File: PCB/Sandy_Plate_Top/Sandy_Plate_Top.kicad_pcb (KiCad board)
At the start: 2 copper layers, 285 x 37.6 mm, 21 parts

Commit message: Top用プレート作成（穴はEdge.Cutじゃない方法で）
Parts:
- removed the SW_=1 at (291.3, 27.0)
- added REF**: MX-Switch-Hole-1u+1u-with-hole, locallib:MX-Switch-Hole-1u+1u-with-hole, F.Cu at (138.9, 27.0)
- added REF**: MX-Switch-Hole, locallib:MX-Switch-Hole, F.Cu at (167.5, 46.1)
- added REF**: MX-Switch-Hole, locallib:MX-Switch-Hole, F.Cu at (91.3, 27.0)
- added REF**: MX-Switch-Hole-1u+1u-with-hole, locallib:MX-Switch-Hole-1u+1u-with-hole, F.Cu at (62.7, 27.0)
- added REF**: MX-Switch-Hole, locallib:MX-Switch-Hole, F.Cu at (224.7, 27.0)
- added REF**: MX-Switch-Hole, locallib:MX-Switch-Hole, F.Cu at (129.4, 46.1)
- added REF**: MX-Switch-Hole, locallib:MX-Switch-Hole, F.Cu at (281.8, 27.0)
- added REF**: MX-Switch-Hole, locallib:MX-Switch-Hole, F.Cu at (148.5, 46.1)
- added REF**: MX-Switch-Hole, locallib:MX-Switch-Hole, F.Cu at (34.2, 27.0)
- added REF**: MX-Switch-Hole-1u+1u-with-hole, locallib:MX-Switch-Hole-1u+1u-with-hole, F.Cu at (253.2, 27.0)
- added REF**: MX-Switch-Hole-1u+1u-with-hole, locallib:MX-Switch-Hole-1u+1u-with-hole, F.Cu at (177.0, 27.0)
- added REF**: MX-Switch-Hole, locallib:MX-Switch-Hole, F.Cu at (167.5, 65.1)
- added REF**: MX-Switch-Hole, locallib:MX-Switch-Hole, F.Cu at (110.4, 27.0)
- added REF**: MX-Switch-Hole, locallib:MX-Switch-Hole, F.Cu at (148.5, 65.1)
- added REF**: MX-Switch-Hole, locallib:MX-Switch-Hole, F.Cu at (205.6, 27.0)
- added REF**: MX-Switch-Hole, locallib:MX-Switch-Hole, F.Cu at (186.6, 46.1)
- added SW_'1: SW_Push, Jones.local:MXOnly-1U-Hotswap-guide-dummy, F.Cu at (167.5, 65.1)
- added SW_;1: SW_Push, Jones.local:MXOnly-1U-Hotswap-guide-dummy, F.Cu at (148.5, 65.1)
- REF**: footprint locallib:60_Outline-Sandy-Plate-Top2-thick-frame -> locallib:60_Outline-Sandy-DN0040-Plate-Top-outer-frame-only
- moved SW_INS1 9.53 mm to (281.8, 27.0)
- moved SW_-1 9.53 mm to (186.6, 27.0)
- moved SW_10 9.53 mm to (262.8, 27.0)
- moved SW_3 9.53 mm to (91.3, 27.0)
- moved SW_4 9.53 mm to (110.4, 27.0)
- moved SW_6 9.53 mm to (167.4, 27.0)
- moved SW_7 9.53 mm to (205.6, 27.0)
- moved SW_9 9.53 mm to (243.7, 27.0)
- moved SW_=1 9.53 mm to (148.5, 27.0)
- moved SW_1 9.52 mm to (53.2, 27.0)
- moved SW_ESC1 9.52 mm to (34.2, 27.0)
- moved SW_2 9.52 mm to (72.3, 27.0)
- moved SW_5 9.52 mm to (129.4, 27.0)
- moved SW_8 9.52 mm to (224.7, 27.0)
- renumbered SW_6 to SW_-1, SW_\1 to SW_6, SW_`1 to SW_=1, SW_-1 to SW_INS1
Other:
- board size 285 x 37.6 mm -> 285 x 56.6 mm
- board text added: "#Sandy_kbd DN0040, Plate for Top by @jpskenn"
- board text removed: "#Sandy_kbd DN0030, Plate for Top by @jpskenn"

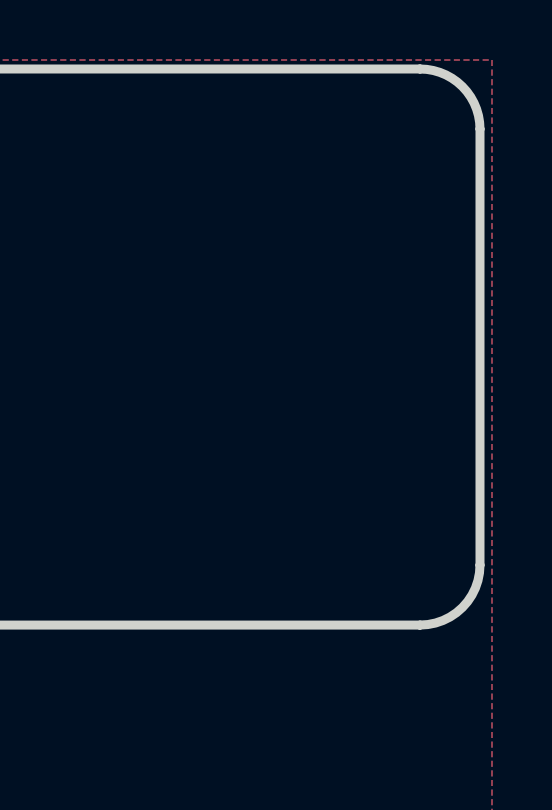
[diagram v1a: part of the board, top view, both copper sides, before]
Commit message: WIP 配線中。ハンダマスクの拡張を変更0.2→0
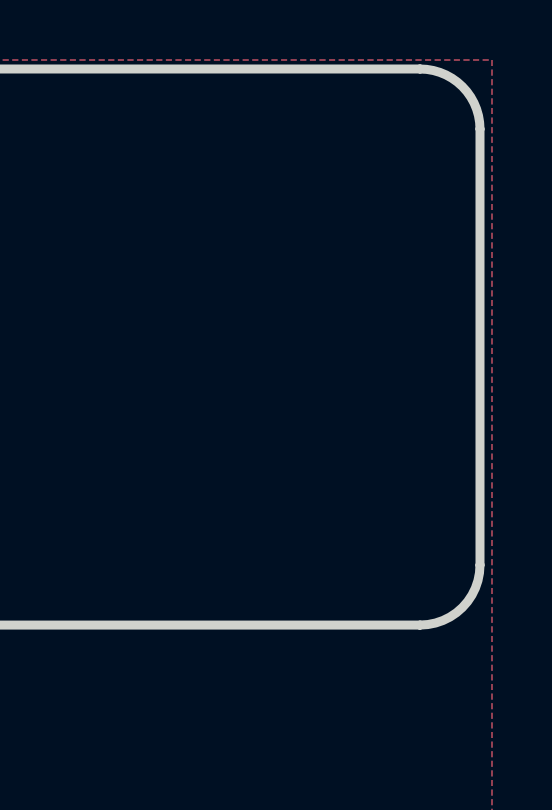
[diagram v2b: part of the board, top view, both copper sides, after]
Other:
- rule pad_to_mask_clearance: 0.2 -> 0
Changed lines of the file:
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@@
 			(dielectric_constraints no)
 		)
-		(pad_to_mask_clearance 0.2)
+		(pad_to_mask_clearance 0)
 		(allow_soldermask_bridges_in_footprints no)
 		(aux_axis_origin 15.10531 17.478405)
@@
 		(fp_arc
 			(start 18.325 20.271492)
-			(mid 18.745535 19.256282)
+			(mid 18.745534 19.256278)
 			(end 19.760746 18.835746)
 			(stroke
@@
 		(fp_arc
 			(start 37.375 1.221492)
-			(mid 37.795526 0.206288)
+			(mid 37.795535 0.206282)
 			(end 38.810746 -0.214254)
 			(stroke
@@
 		(fp_arc
 			(start 140.475 -18.75004)
-			(mid 141.889257 -18.164285)
+			(mid 141.889222 -18.164279)
 			(end 142.475 -16.75004)
 			(stroke
@@
 		(fp_arc
 			(start 142.475 -2.214254)
-			(mid 141.889197 -0.80007)
+			(mid 141.889203 -0.800035)
 			(end 140.475 -0.214254)
 			(stroke
